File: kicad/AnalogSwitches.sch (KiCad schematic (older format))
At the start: 70 parts

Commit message: Using ERF32FG12 SoC instead of PIC32MX
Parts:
- removed P?: TX_VCC, Connectors_Samtec:SL-102-X-XX_1x02, symbol RCTX-rescue:Conn_01x02-conn
- removed P?: SWITCHES, Connectors_Samtec:SL-108-X-XX_1x08, symbol RCTX-rescue:Conn_01x08-conn
- removed P?: PWR_BUS, Connectors_Samtec:SL-104-X-XX_1x04, symbol RCTX-rescue:Conn_01x04-conn
- removed P?: KEYPAD, Connectors_Samtec:SL-102-X-XX_1x02, symbol RCTX-rescue:Conn_01x02-conn
- removed P?: SW, symbol conn:Conn_01x02
- added P?: KEYPAD, symbol conn:Conn_02x03_Odd_Even
- added P?: SWITCHES, symbol conn:Conn_02x08_Odd_Even
- added P?: SW, symbol conn:Conn_02x02_Odd_Even
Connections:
- net labels added: CABLE_MODE, MASTER, RADIO_MODE, SLAVE
- wire segments 244 -> 270
- no-connect marks 8 -> 3
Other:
- note removed: "+3.3V"
- note removed: "+5V"
- note removed: "GND"
- note removed: "VBAT+"
- note removed: "from TXM (RF MODULE VCC)"
- note removed: "to TXM (RF MODULE VCC)"
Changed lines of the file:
@@
 $Descr A4 8268 11693 portrait
 encoding utf-8
-Sheet 12 13
+Sheet 9 10
 Title ""
 Date ""
@@
 	2000 1250 2000 1500
 Wire Wire Line
-	3800 7400 3800 7800
-$Comp
-L RCTX-rescue:Conn_01x02-conn P?
-U 1 1 600F86D5
-P 3900 8000
-AR Path="/600F86D5" Ref="P?"  Part="1"
-AR Path="/4C8BDE8D/600F86D5" Ref="P?"  Part="1"
-AR Path="/5FF689BA/600F86D5" Ref="P?"  Part="1"
-F 0 "P?" H 3850 7800 50  0000 L CNN
-F 1 "TX_VCC" V 4000 7800 50  0000 L CNN
-F 2 "Connectors_Samtec:SL-102-X-XX_1x02" H 3900 8000 50  0001 C CNN
-F 3 "~" H 3900 8000 50  0001 C CNN
-	1    3900 8000
-	0    1    1    0
-$EndComp
-Text Notes 3850 8150 3    50   ~ 0
-to TXM (RF MODULE VCC)
-Text Notes 3950 8150 3    50   ~ 0
-from TXM (RF MODULE VCC)
-Wire Wire Line
-	3900 7800 3900 6850
-Wire Wire Line
-	3900 6850 3700 6850
-Wire Wire Line
 	3700 6850 3700 7000
 $Comp
@@
 AR Path="/5FF689BA/600F86E0" Ref="SW?"  Part="1"
 F 0 "SW?" H 3550 7300 50  0000 C CNN
-F 1 "RF_SW" H 4150 7250 50  0000 C CNN
+F 1 "RF_SW" H 3700 7400 50  0000 C CNN
 F 2 "Buttons_Switches_THT:SW_CuK_JS202011AQN_DPDT_Angled" H 3075 7375 50  0001 C CNN
 F 3 "" H 3075 7375 50  0001 C CNN
@@
 Wire Notes Line
 	3350 7200 3750 7200
-NoConn ~ 3700 7400
 NoConn ~ 3600 7400
 Wire Notes Line
@@
 AR Path="/5FF689BA/6016949E" Ref="SW?"  Part="1"
 F 0 "SW?" H 2650 7300 50  0000 C CNN
-F 1 "SW_NC" H 3250 7200 50  0000 C CNN
+F 1 "SW_NC" H 2800 7400 50  0000 C CNN
 F 2 "Buttons_Switches_THT:SW_CuK_JS202011AQN_DPDT_Angled" H 2175 7375 50  0001 C CNN
 F 3 "" H 2175 7375 50  0001 C CNN
@@
 Wire Notes Line
 	2450 7200 2850 7200
-NoConn ~ 2800 7400
-NoConn ~ 2700 7400
 Wire Notes Line
 	2950 6950 2200 6950
@@
 Wire Wire Line
 	5500 9600 6400 9600
-Connection ~ 1200 10850
-Wire Wire Line
-	1200 10850 1200 10950
 $Comp
 L RCTX-rescue:GND-power #PWR?
@@
 	1    0    0    -1
 $EndComp
-$Comp
-L RCTX-rescue:Conn_01x04-conn P?
-U 1 1 602DC4AA
-P 2750 10750
-AR Path="/4C8BDF50/602DC4AA" Ref="P?"  Part="1"
-AR Path="/5FF689BA/602DC4AA" Ref="P?"  Part="1"
-F 0 "P?" H 2700 10450 50  0000 L CNN
-F 1 "PWR_BUS" V 2850 10550 50  0000 L CNN
-F 2 "Connectors_Samtec:SL-104-X-XX_1x04" H 2750 10750 50  0001 C CNN
-F 3 "~" H 2750 10750 50  0001 C CNN
-	1    2750 10750
-	1    0    0    -1
-$EndComp
-Text Notes 2950 11000 0    60   ~ 0
-VBAT+
-Text Notes 2950 10800 0    60   ~ 0
-+5V
-Text Notes 2950 10900 0    60   ~ 0
-GND
-Text Notes 3200 10700 2    60   ~ 0
-+3.3V
 Wire Wire Line
 	1200 10350 1300 10350
 Wire Wire Line
-	2550 10250 2200 10250
-Wire Wire Line
-	2200 10250 2200 10650
-Wire Wire Line
-	2200 10650 1700 10650
-Wire Wire Line
-	1700 10350 2100 10350
-Wire Wire Line
-	2100 10350 2100 10150
-Wire Wire Line
-	2100 10150 2550 10150
-Wire Wire Line
-	2550 10850 1200 10850
-Wire Wire Line
-	1200 10850 1200 10650
+	1900 10450 1800 10450
+Wire Wire Line
+	1800 10450 1800 10650
+Wire Wire Line
+	1800 10650 1700 10650
 Wire Wire Line
 	1200 10650 1300 10650
 Connection ~ 1200 10650
-Text Notes 2950 10300 0    60   ~ 0
+Text Notes 2600 10500 0    60   ~ 0
 PB_RIGHT
-Text Notes 2950 10200 0    60   ~ 0
+Text Notes 2600 10400 0    60   ~ 0
 PB_LEFT
-NoConn ~ 2550 10950
-NoConn ~ 2550 10750
 $Comp
 L RCTX-rescue:SW_SPST-switches SW?
@@
 Wire Wire Line
 	1200 10650 1200 10350
-$Comp
-L RCTX-rescue:Conn_01x08-conn P?
-U 1 1 602DC3C3
+Wire Wire Line
+	3950 1250 3950 1350
+Wire Wire Line
+	3400 1250 3950 1250
+Wire Wire Line
+	4150 1250 4150 1350
+Wire Wire Line
+	4150 1250 4750 1250
+$Comp
+L conn:Conn_02x03_Odd_Even P?
+U 1 1 621405B6
+P 4050 1550
+F 0 "P?" V 4047 1730 60  0000 L CNN
+F 1 "KEYPAD" V 4153 1730 60  0000 L CNN
+F 2 "" H 4050 1550 50  0001 C CNN
+F 3 "~" H 4050 1550 50  0001 C CNN
+	1    4050 1550
+	0    1    1    0
+$EndComp
+$Comp
+L power:+3.3V #PWR?
+U 1 1 6216157C
+P 4050 750
+F 0 "#PWR?" H 4050 600 50  0001 C CNN
+F 1 "+3.3V" H 4065 923 50  0000 C CNN
+F 2 "" H 4050 750 50  0001 C CNN
+F 3 "" H 4050 750 50  0001 C CNN
+	1    4050 750
+	1    0    0    -1
+$EndComp
+Wire Wire Line
+	4050 1350 4050 750
+Wire Wire Line
+	3950 1850 3950 1950
+Wire Wire Line
+	3950 1950 4050 1950
+Wire Wire Line
+	4050 1950 4050 1850
+Wire Wire Line
+	4050 1950 4150 1950
+Wire Wire Line
+	4150 1950 4150 1850
+Connection ~ 4050 1950
+$Comp
+L power:GND #PWR?
+U 1 1 62194603
+P 4050 2050
+F 0 "#PWR?" H 4050 1800 50  0001 C CNN
+F 1 "GND" H 4055 1877 50  0000 C CNN
+F 2 "" H 4050 2050 50  0001 C CNN
+F 3 "" H 4050 2050 50  0001 C CNN
+	1    4050 2050
+	-1   0    0    -1
+$EndComp
+Wire Wire Line
+	4050 2050 4050 1950
+$Comp
+L conn:Conn_02x08_Odd_Even P?
+U 1 1 621AA0DF
 P 1450 9200
-AR Path="/4C8BDF50/602DC3C3" Ref="P?"  Part="1"
-AR Path="/5FF689BA/602DC3C3" Ref="P?"  Part="1"
-F 0 "P?" H 1450 8700 60  0000 C CNN
-F 1 "SWITCHES" V 1550 9200 60  0000 C CNN
-F 2 "Connectors_Samtec:SL-108-X-XX_1x08" H 1450 9200 50  0001 C CNN
-F 3 "" H 1450 9200 50  0001 C CNN
+F 0 "P?" H 1500 8600 60  0000 C CNN
+F 1 "SWITCHES" H 1500 9900 60  0000 C CNN
+F 2 "" H 1450 9200 50  0001 C CNN
+F 3 "~" H 1450 9200 50  0001 C CNN
 	1    1450 9200
 	-1   0    0    -1
 $EndComp
-$Comp
-L RCTX-rescue:Conn_01x02-conn P?
-U 1 1 6083DFDA
-P 4000 1550
-AR Path="/6083DFDA" Ref="P?"  Part="1"
-AR Path="/4C8BDE8D/6083DFDA" Ref="P?"  Part="1"
-AR Path="/5FF689BA/6083DFDA" Ref="P?"  Part="1"
-F 0 "P?" H 3950 1350 50  0000 L CNN
-F 1 "KEYPAD" V 4100 1350 50  0000 L CNN
-F 2 "Connectors_Samtec:SL-102-X-XX_1x02" H 4000 1550 50  0001 C CNN
-F 3 "~" H 4000 1550 50  0001 C CNN
-	1    4000 1550
-	0    -1   1    0
-$EndComp
-Wire Wire Line
-	4000 1250 4000 1350
-Wire Wire Line
-	3400 1250 4000 1250
-Wire Wire Line
-	4100 1250 4100 1350
-Wire Wire Line
-	4100 1250 4750 1250
-$Comp
-L power:+3.3V #PWR?
-U 1 1 608CF11F
-P 2450 10550
-F 0 "#PWR?" H 2450 10400 50  0001 C CNN
-F 1 "+3.3V" H 2465 10723 50  0000 C CNN
-F 2 "" H 2450 10550 50  0001 C CNN
-F 3 "" H 2450 10550 50  0001 C CNN
-	1    2450 10550
-	-1   0    0    -1
-$EndComp
-Wire Wire Line
-	2550 10650 2450 10650
-Wire Wire Line
-	2450 10650 2450 10550
-$Comp
-L conn:Conn_01x02 P?
-U 1 1 60A7F950
-P 2750 10150
-F 0 "P?" H 2700 9950 50  0000 L CNN
-F 1 "SW" V 2850 10050 50  0000 L CNN
-F 2 "" H 2750 10150 50  0001 C CNN
-F 3 "~" H 2750 10150 50  0001 C CNN
-	1    2750 10150
-	1    0    0    -1
-$EndComp
+Wire Wire Line
+	1150 8900 1050 8900
+Wire Wire Line
+	1050 8900 1050 9000
+Wire Wire Line
+	1050 9000 1150 9000
+Wire Wire Line
+	1050 9000 1050 9100
+Wire Wire Line
+	1050 9100 1150 9100
+Connection ~ 1050 9000
+Wire Wire Line
+	1050 9100 1050 9200
+Wire Wire Line
+	1050 9200 1150 9200
+Connection ~ 1050 9100
+Wire Wire Line
+	1050 9200 1050 9300
+Wire Wire Line
+	1050 9300 1150 9300
+Connection ~ 1050 9200
+Wire Wire Line
+	1050 9300 1050 9400
+Wire Wire Line
+	1050 9400 1150 9400
+Connection ~ 1050 9300
+Wire Wire Line
+	1050 9400 1050 9500
+Wire Wire Line
+	1050 9500 1150 9500
+Connection ~ 1050 9400
+Wire Wire Line
+	1050 9600 1150 9600
+$Comp
+L RCTX-rescue:GND-power #PWR?
+U 1 1 62244791
+P 1050 9700
+AR Path="/4C8BDF50/62244791" Ref="#PWR?"  Part="1"
+AR Path="/5FF689BA/62244791" Ref="#PWR?"  Part="1"
+F 0 "#PWR?" H 1050 9450 50  0001 C CNN
+F 1 "GND" H 1055 9527 50  0000 C CNN
+F 2 "" H 1050 9700 50  0001 C CNN
+F 3 "" H 1050 9700 50  0001 C CNN
+	1    1050 9700
+	1    0    0    -1
+$EndComp
+Wire Wire Line
+	1050 9500 1050 9600
+Connection ~ 1050 9500
+Connection ~ 1050 9600
+Wire Wire Line
+	1050 9600 1050 9700
+Wire Wire Line
+	1200 10650 1200 10850
+Wire Wire Line
+	1700 10350 1900 10350
+$Comp
+L conn:Conn_02x02_Odd_Even P?
+U 1 1 622F96E2
+P 2100 10350
+F 0 "P?" H 2150 10589 60  0000 C CNN
+F 1 "SW" H 2150 10483 60  0000 C CNN
+F 2 "" H 2100 10350 50  0001 C CNN
+F 3 "~" H 2100 10350 50  0001 C CNN
+	1    2100 10350
+	1    0    0    -1
+$EndComp
+Wire Wire Line
+	2400 10350 2500 10350
+Wire Wire Line
+	2500 10350 2500 10450
+Wire Wire Line
+	2500 10450 2400 10450
+Wire Wire Line
+	2500 10450 2500 10850
+Wire Wire Line
+	2500 10850 1200 10850
+Connection ~ 2500 10450
+Connection ~ 1200 10850
+Wire Wire Line
+	1200 10850 1200 10950
+Wire Wire Line
+	3700 6850 2800 6850
+Wire Wire Line
+	2800 6850 2800 7000
+Text GLabel 3800 7600 3    50   Input ~ 0
+RADIO_MODE
+Wire Wire Line
+	3800 7400 3800 7600
+Text GLabel 2800 7600 3    50   Input ~ 0
+MASTER
+Text GLabel 2900 7600 3    50   Input ~ 0
+SLAVE
+Text GLabel 3700 7600 3    50   Input ~ 0
+CABLE_MODE
+Wire Wire Line
+	3700 7400 3700 7600
+Wire Wire Line
+	2900 7400 2900 7600
+Wire Wire Line
+	2800 7400 2800 7600
 $EndSCHEMATC

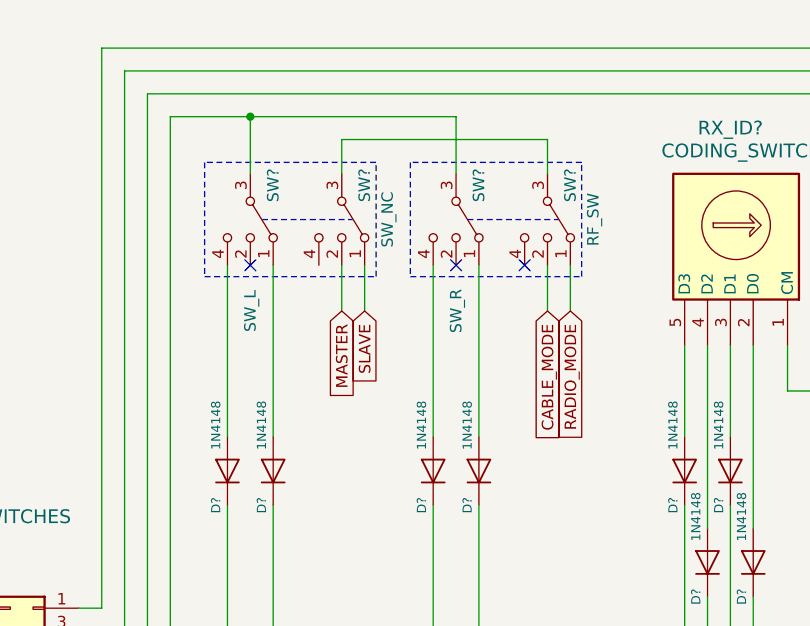
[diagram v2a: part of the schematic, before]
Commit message: Using ERF32FG12 SoC instead of PIC32MX
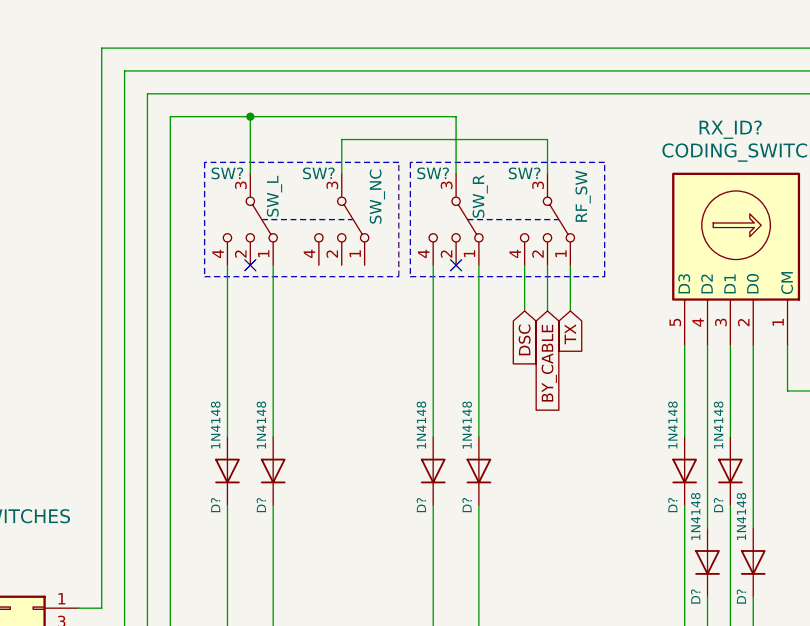
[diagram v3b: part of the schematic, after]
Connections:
- net labels added: BY_CABLE, DSC, TX
- net labels removed: CABLE_MODE, MASTER, RADIO_MODE, SLAVE
- wire segments 270 -> 269
- no-connect marks 3 -> 2
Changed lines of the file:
@@
 $Descr A4 8268 11693 portrait
 encoding utf-8
-Sheet 9 5
+Sheet 4 5
 Title ""
 Date ""
@@
 AR Path="/4C8BDE8D/600F86E0" Ref="SW?"  Part="1"
 AR Path="/5FF689BA/600F86E0" Ref="SW?"  Part="1"
-F 0 "SW?" H 3550 7300 50  0000 C CNN
-F 1 "RF_SW" H 3700 7400 50  0000 C CNN
+F 0 "SW?" V 3500 7100 50  0000 C CNN
+F 1 "RF_SW" H 3600 7350 50  0000 C CNN
 F 2 "Buttons_Switches_THT:SW_CuK_JS202011AQN_DPDT_Angled" H 3075 7375 50  0001 C CNN
 F 3 "" H 3075 7375 50  0001 C CNN
@@
 AR Path="/4C8BDE8D/600F86E6" Ref="SW?"  Part="1"
 AR Path="/5FF689BA/600F86E6" Ref="SW?"  Part="1"
-F 0 "SW?" H 3150 7300 50  0000 C CNN
-F 1 "SW_R" H 3700 7200 50  0000 C CNN
+F 0 "SW?" V 3100 7100 50  0000 C CNN
+F 1 "SW_R" H 3200 7300 50  0000 C CNN
 F 2 "Buttons_Switches_THT:SW_CuK_JS202011AQN_DPDT_Angled" H 2675 7375 50  0001 C CNN
 F 3 "" H 2675 7375 50  0001 C CNN
@@
 Wire Notes Line
 	3350 7200 3750 7200
-NoConn ~ 3600 7400
 Wire Notes Line
-	3850 6950 3100 6950
+	3950 6950 3100 6950
 Wire Notes Line
 	3100 6950 3100 7450
 Wire Notes Line
-	3100 7450 3850 7450
+	3100 7450 3950 7450
 Wire Notes Line
-	3850 7450 3850 6950
+	3950 7450 3950 6950
 Wire Wire Line
 	2400 6750 2400 7000
@@
 AR Path="/4C8BDE8D/6016949E" Ref="SW?"  Part="1"
 AR Path="/5FF689BA/6016949E" Ref="SW?"  Part="1"
-F 0 "SW?" H 2650 7300 50  0000 C CNN
-F 1 "SW_NC" H 2800 7400 50  0000 C CNN
+F 0 "SW?" V 2600 7100 50  0000 C CNN
+F 1 "SW_NC" H 2700 7350 50  0000 C CNN
 F 2 "Buttons_Switches_THT:SW_CuK_JS202011AQN_DPDT_Angled" H 2175 7375 50  0001 C CNN
 F 3 "" H 2175 7375 50  0001 C CNN
@@
 AR Path="/4C8BDE8D/601694A4" Ref="SW?"  Part="1"
 AR Path="/5FF689BA/601694A4" Ref="SW?"  Part="1"
-F 0 "SW?" H 2250 7300 50  0000 C CNN
-F 1 "SW_L" H 2800 7200 50  0000 C CNN
+F 0 "SW?" V 2200 7100 50  0000 C CNN
+F 1 "SW_L" H 2300 7300 50  0000 C CNN
 F 2 "Buttons_Switches_THT:SW_CuK_JS202011AQN_DPDT_Angled" H 1775 7375 50  0001 C CNN
 F 3 "" H 1775 7375 50  0001 C CNN
@@
 	2450 7200 2850 7200
 Wire Notes Line
-	2950 6950 2200 6950
+	3050 6950 2200 6950
 Wire Notes Line
 	2200 6950 2200 7450
 Wire Notes Line
-	2200 7450 2950 7450
+	2200 7450 3050 7450
 Wire Notes Line
-	2950 7450 2950 6950
+	3050 7450 3050 6950
 Wire Wire Line
 	5400 1250 5650 1250
@@
 	2800 6850 2800 7000
 Text GLabel 3800 7600 3    50   Input ~ 0
-RADIO_MODE
+TX
 Wire Wire Line
 	3800 7400 3800 7600
-Text GLabel 2800 7600 3    50   Input ~ 0
-MASTER
-Text GLabel 2900 7600 3    50   Input ~ 0
-SLAVE
+Text GLabel 3600 7600 3    50   Input ~ 0
+DSC
+Wire Wire Line
+	3700 7400 3700 7600
 Text GLabel 3700 7600 3    50   Input ~ 0
-CABLE_MODE
-Wire Wire Line
-	3700 7400 3700 7600
-Wire Wire Line
-	2900 7400 2900 7600
-Wire Wire Line
-	2800 7400 2800 7600
+BY_CABLE
+Wire Wire Line
+	3600 7600 3600 7400
 $EndSCHEMATC

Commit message: Using Pic16(L)F1459 as USB->(UART/SWD/I2C) bridge
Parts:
- removed D? (x4): 1N4148, Diodes_THT:D_5W_P5.08mm_Vertical_KathodeUp, symbol RCTX-rescue:D-device
- removed P?: SWITCHES, symbol conn:Conn_02x08_Odd_Even
- removed RF_BAND?: CODING_SWITCH, Buttons_Switches_THT:Nidec_Copal_SH-7010C, symbol RCTX-rescue:SW_Coded-switches
- removed SW?: PB_LEFT, Buttons_Switches_THT:SW_PUSH_6mm_h5mm, symbol RCTX-rescue:SW_SPST-switches
- removed SW?: PB_RIGHT, Buttons_Switches_THT:SW_PUSH_6mm_h5mm, symbol RCTX-rescue:SW_SPST-switches
- added P?: SWITCHES, symbol conn:Conn_02x09_Odd_Even
- added SW?: PB_LEFT, symbol RCTX-rescue:SW_Push-switches
- added SW?: PB_RIGHT, symbol RCTX-rescue:SW_Push-switches
- HEX_SW?: renamed from RX_SUB_ID?; value CODING_SWITCH -> RX_SUB_ID
- HEX_SW?: renamed from RX_ID?; value CODING_SWITCH -> RX_ID
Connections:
- net labels removed: BY_CABLE, DSC, TX
- wire segments 269 -> 254
- no-connect marks 2 -> 3
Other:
- moved on the sheet: D?, RX_ID?, RX_SUB_ID?
